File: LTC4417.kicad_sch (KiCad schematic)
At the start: 33 parts, among them Q1 IRF7324, Q2 IRF7324, Q3 IRF7324, U1 LTC4417CGN

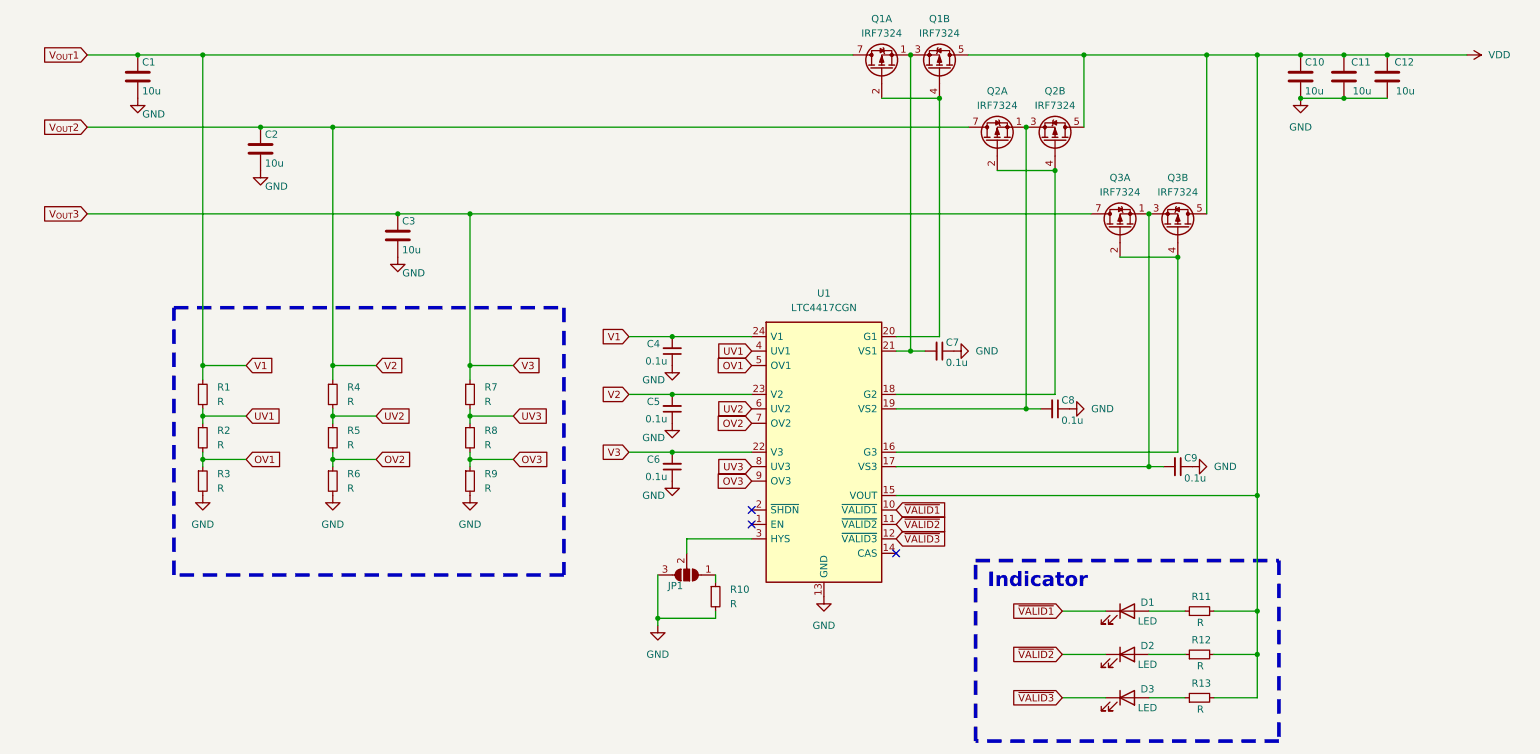
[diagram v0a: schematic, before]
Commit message: add footprint 18650 batteryClip
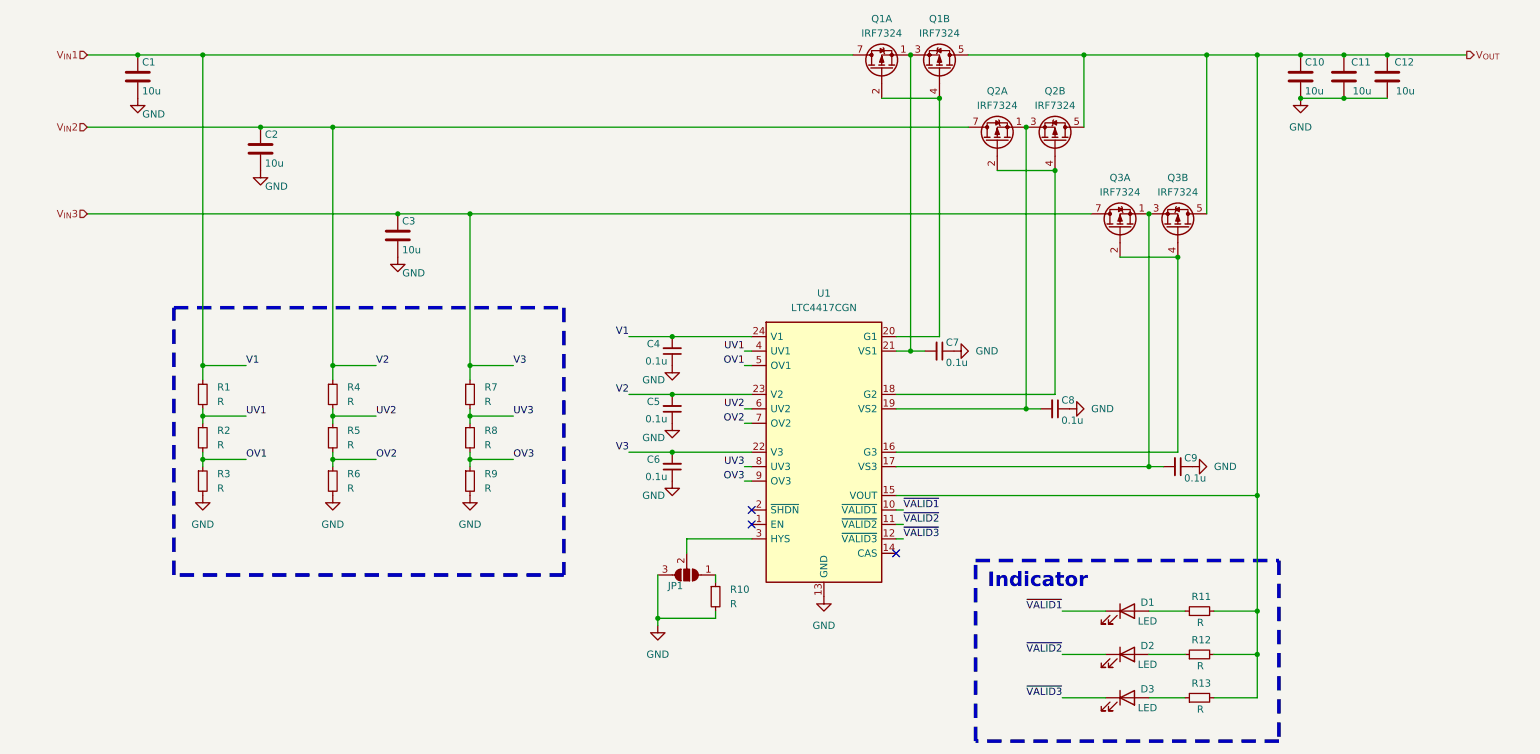
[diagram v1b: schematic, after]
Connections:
- net V1 renamed V_{IN}1
- net V2 renamed V_{IN}2
- net V3 renamed V_{IN}3
- net VDD renamed V_{OUT}
